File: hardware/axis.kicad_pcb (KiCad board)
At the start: 4 copper layers, 66 x 17.5 mm, 43 parts, among them J101 CORTEX-DEBUG, J102 JAE_DX07S016JA3, SW101 SW_Push, SW102 SW_Push, U101 TPS78433QWDRBRQ1, U102 ATSAMD51G, U103 BMM150, U104 BHI160, Y101 32k768

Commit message: Update parts
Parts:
- C101, C108, C109, C110, C112: footprint Capacitor_SMD:C_0603_1608Metric -> V2_Capacitor_SMD:C_0603
- C102, C103, C104, C105, C111: value 0u1 -> 1u; footprint Capacitor_SMD:C_0603_1608Metric -> V2_Capacitor_SMD:C_0603
- C106, C107: footprint Capacitor_SMD:C_0805_2012Metric -> V2_Capacitor_SMD:C_0805
- D103: footprint LED_SMD:LED_0603_1608Metric -> V2_LED:LED_0603
- FID101, FID102, FID103: value Fiducial -> Fiducial_Paste
- INFO102: value ORDER-NUMBER -> Order_Number
- J101: value CORTEX-DEBUG -> Cortex_Debug
- J102: value JAE_DX07S016JA3 -> DX07S016JA3
- R101, R102, R103, R104, R105, R106, R107, R108: footprint Resistor_SMD:R_0603_1608Metric -> V2_Resistor_SMD:R_0603
- SW101, SW102: value SW_Push -> SKSG
- moved INFO101 2.00 mm to (124.5, 114.2)
- moved ICON101 0.75 mm to (169.8, 99.8)
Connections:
- net USB-Shield renamed Shield
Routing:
- net GND: vias 89 -> 69

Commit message: Update library
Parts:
- J101: value Cortex_Debug -> Cortex; footprint V2_Cortex_Debug:Cortex_Debug_Pad -> V2_Connector_Debug:Cortex
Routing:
- net GND: vias 69 -> 67
- net +3V3: vias 18 -> 17

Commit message: Use date as revision
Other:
- board text added: "2026-02-07 stencil"

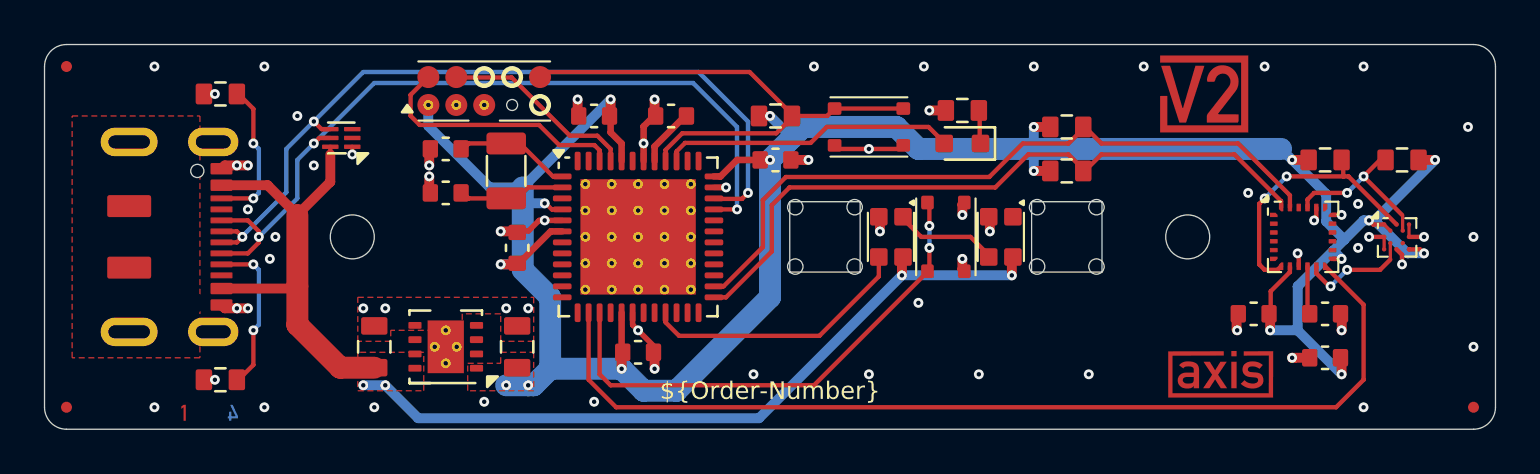
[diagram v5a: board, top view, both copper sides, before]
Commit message: Replace Order_Number
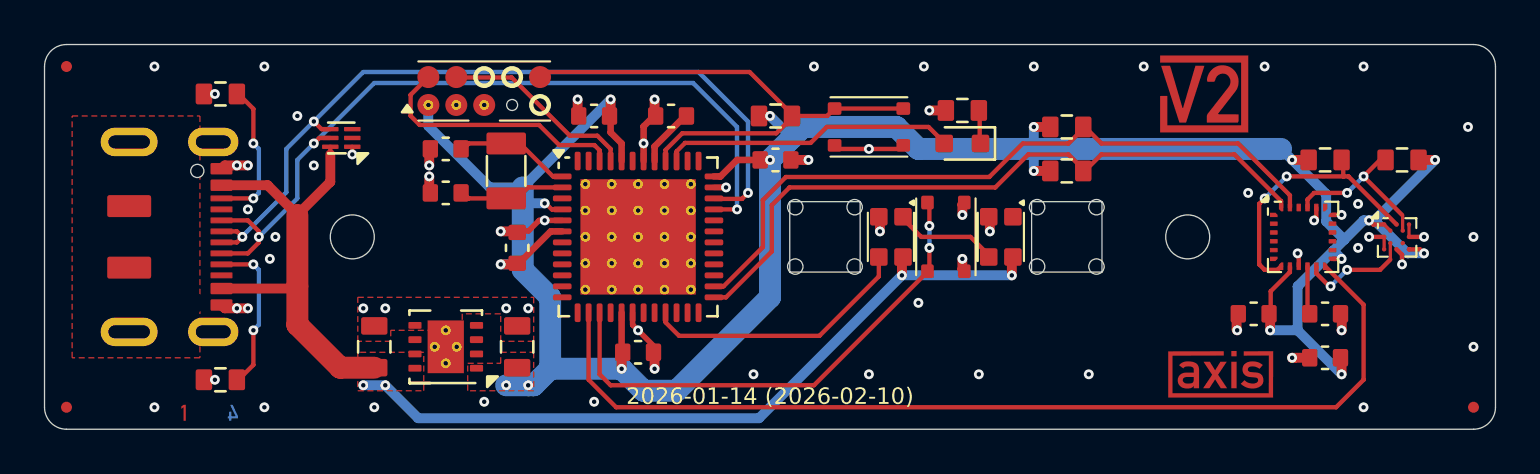
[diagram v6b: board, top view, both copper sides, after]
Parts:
- H101, H102: value MountingHole_2mm -> 2mm
- INFO102: value Order_Number -> ~; footprint V2_Production:Order_Number -> V2_Production:Revision
- moved INFO102 0.25 mm to (150.0, 113.5)

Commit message: Update
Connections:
- net /Aux-SCK renamed /Aux-SCL
- net /SCK renamed /SCL
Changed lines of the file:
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@@
 	(net 54 "unconnected-(U102-PA20-Pad29)")
 	(net 55 "unconnected-(U102-PA21-Pad30)")
-	(net 56 "/SCK")
+	(net 56 "/SCL")
 	(net 57 "/Aux-SDA")
-	(net 58 "/Aux-SCK")
+	(net 58 "/Aux-SCL")
 	(net 59 "/Button")
 	(net 60 "/Interrupt")
@@
 			(layers "F.Cu" "F.Mask")
 			(roundrect_rratio 0.1333333333)
-			(net 58 "/Aux-SCK")
+			(net 58 "/Aux-SCL")
 			(pintype "passive")
 		)
@@
 			(layers "F.Cu" "F.Mask" "F.Paste")
 			(roundrect_rratio 0.3)
-			(net 56 "/SCK")
+			(net 56 "/SCL")
 			(pinfunction "PA17")
 			(pintype "bidirectional")
@@
 			(property pad_prop_bga)
 			(layers "F.Cu" "F.Mask" "F.Paste")
-			(net 58 "/Aux-SCK")
+			(net 58 "/Aux-SCL")
 			(pinfunction "SCK")
 			(pintype "input")
@@
 			(layers "F.Cu" "F.Mask")
 			(roundrect_rratio 0.1333333333)
-			(net 56 "/SCK")
+			(net 56 "/SCL")
 			(pintype "passive")
 		)
@@
 			(chamfer_ratio 0.5)
 			(chamfer top_left)
-			(net 58 "/Aux-SCK")
+			(net 58 "/Aux-SCL")
 			(pinfunction "ASCK")
 			(pintype "bidirectional")
@@
 			(chamfer_ratio 0.2)
 			(chamfer)
-			(net 56 "/SCK")
+			(net 56 "/SCL")
 			(pinfunction "SCK")
 			(pintype "bidirectional")
